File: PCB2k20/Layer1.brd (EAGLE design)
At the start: 173.9 x 196 mm, 242 parts, among them J1 XT30PB-F, Q1M1 AOD482, Q1M2 AOD482, Q1M3 AOD482, Q1M4 AOD482, U1M1 VNH5019, U1M2 VNH5019, U1M3 VNH5019, U1M4 VNH5019

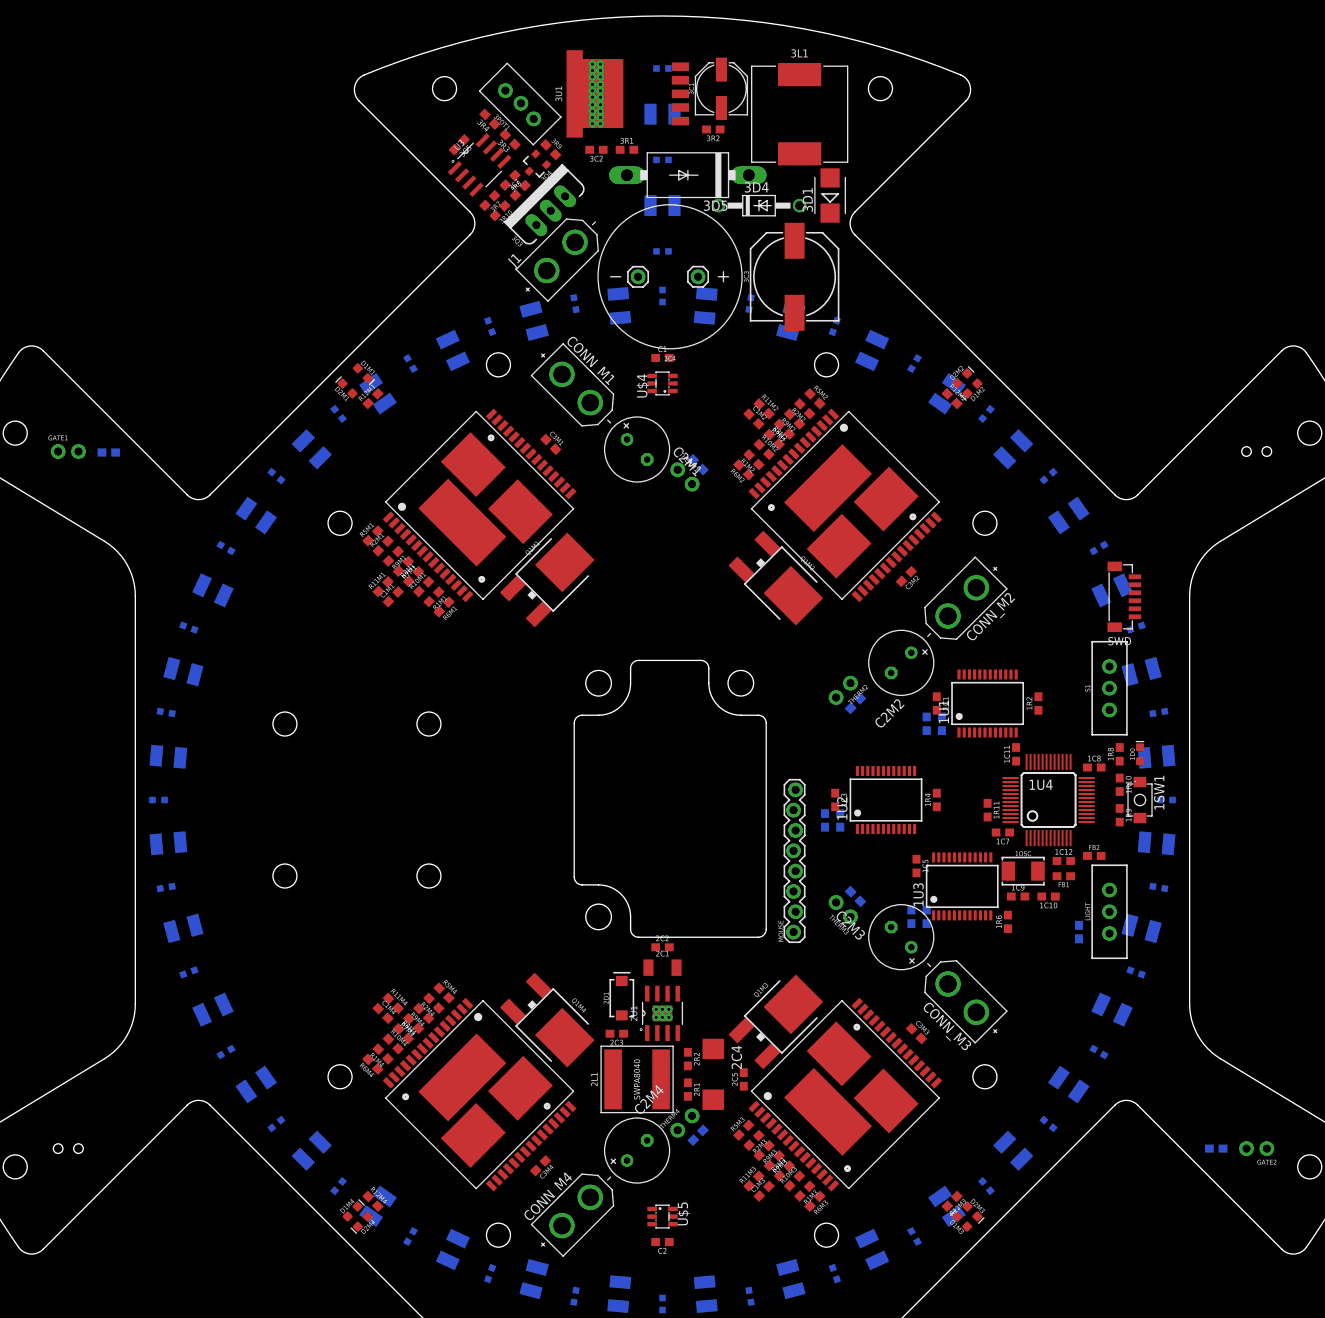
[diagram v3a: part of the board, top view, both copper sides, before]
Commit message: half routed
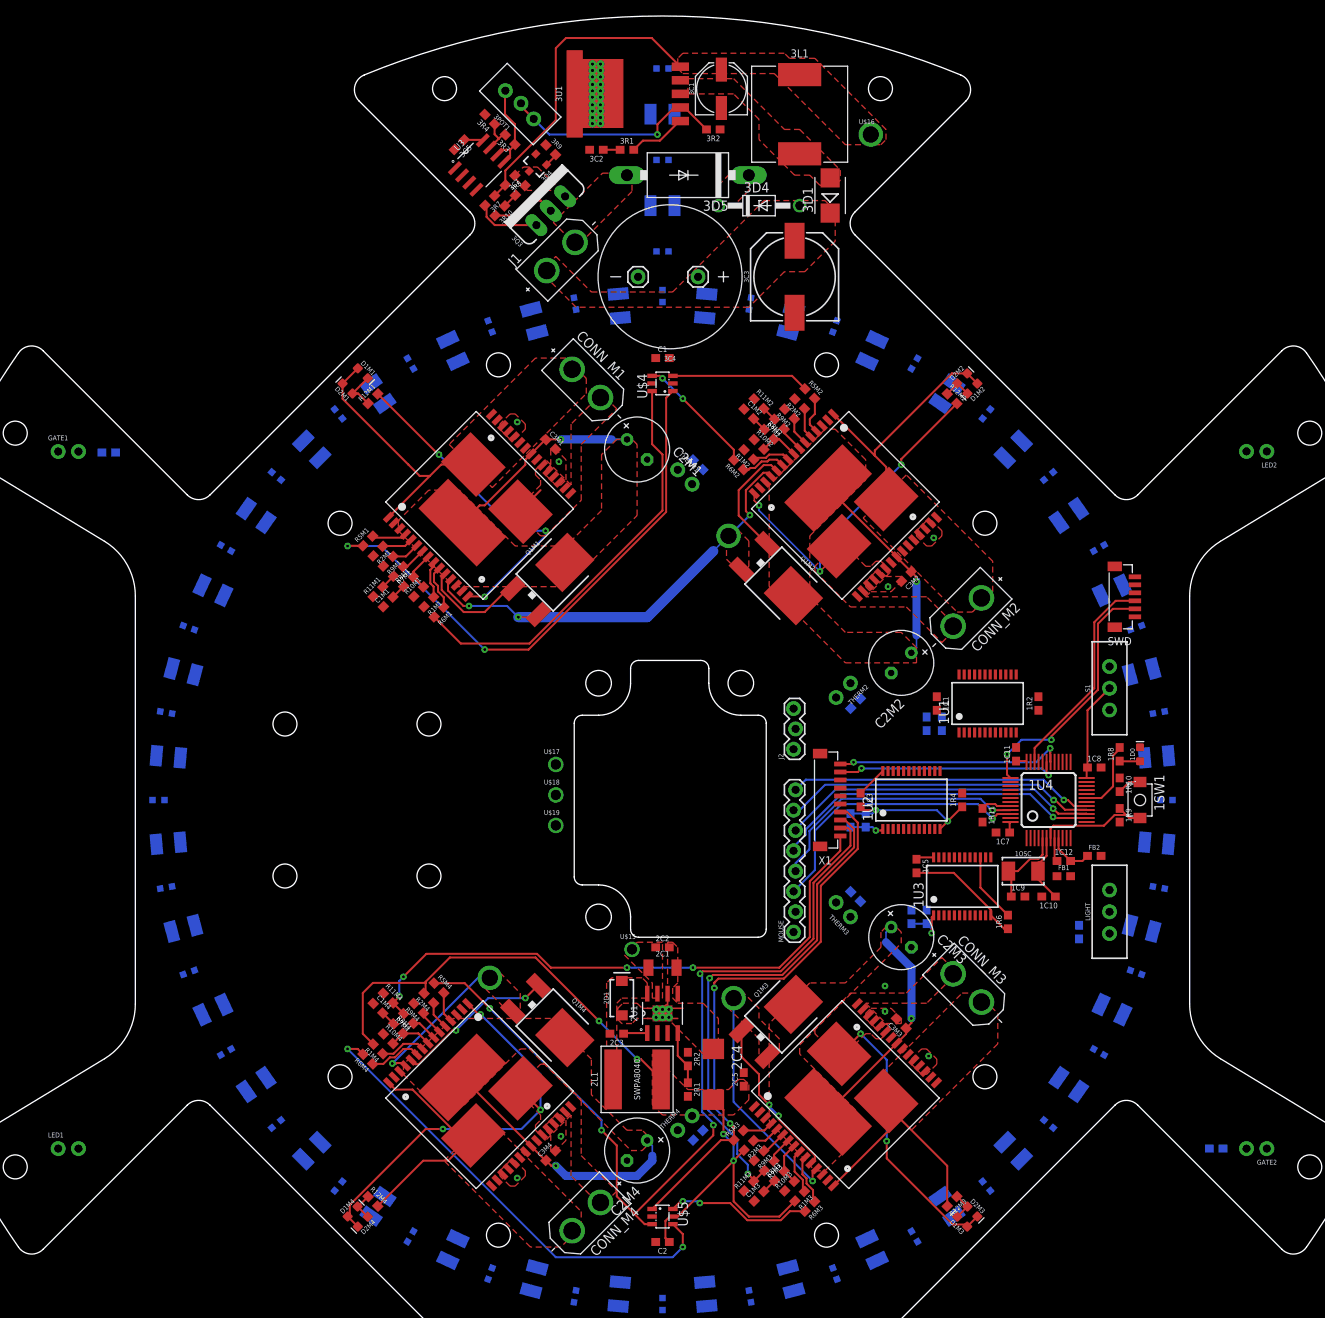
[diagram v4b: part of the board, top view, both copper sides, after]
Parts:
- added J2: CONN_03, JH:1X03_LOCK
- added J3, J4, J5, U$16: 14AWG, JH:14AWG
- added LED1, LED2: (no value), SparkFun-Connectors:1X02_NO_SILK
- added U$15, U$17, U$18, U$19: 18AWG, JH:18AWG
- added X1: BM10B-SRSS-TB, con-JST SH:BM10B-SRSS-TB
- moved 1R4 3.18 mm to (37.5, 0.00)
- moved 1C3 3.18 mm to (24.8, 0.00)
- moved 1R5 3.18 mm to (23.5, -2.54)
- moved 1C4 3.17 mm to (25.4, -2.54)
- moved 1U2 3.17 mm to (31.1, 0.00)
- moved C3M3 2.29 mm to (29.8, -27.9), turned to 135 degrees
- moved C3M4 1.80 mm to (-14.0, -44.5), turned to 45 degrees
- moved CONN_M1 1.42 mm to (-9.53, 52.1)
- moved CONN_M2 1.42 mm to (38.1, 23.5)
- moved CONN_M3 1.42 mm to (38.1, -23.5), turned to 315 degrees
- moved CONN_M4 1.42 mm to (-9.53, -52.1), turned to 225 degrees
- moved C1M4 0.90 mm to (-35.6, -26.0)
- moved R11M1 0.90 mm to (-35.6, 26.0)
- moved R1M4 0.90 mm to (-35.6, -31.1)
- moved R2M1 0.90 mm to (-35.6, 31.1), turned to 225 degrees
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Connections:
- new net LIGHT_INT: J2.1
- net 12V: now also U$15.P$1; no longer 3R7.1, 3R8.2
- net 3.3V: now also J2.3
- net GND: now also J2.2, LED1.2, LED2.2, U$18.P$1
- net INM1: now also X1.8
- net INM2: now also X1.6
- net INM3: now also X1.4
- net INM4: now also X1.2
- net MOUSE_MOT: now also 1U4.45
- net MOUSE_RST: now also 1U4.46
- net N$1: now also LED1.1, LED2.1, U$17.P$1
- net PWMM1: now also X1.7
- net PWMM2: now also X1.5
- net PWMM3: now also X1.3
- net PWMM4: now also X1.1
- net RX: now also X1.9
- net TX: now also X1.10
- net VCCA: now also U$19.P$1
- net VCC_1: now also 3R7.1, 3R8.2, J3.P$1, J4.P$1, J5.P$1, U$16.P$1
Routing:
- net VCC_1: track 0.00 -> 142.9 mm, vias 0 -> 5
- net INM4: track 0.00 -> 111.8 mm, vias 0 -> 4
- net 3.3V: track 0.00 -> 95.5 mm, vias 0 -> 4
- net PWMM4: track 0.00 -> 74.1 mm, vias 0 -> 4
- net INM1: track 0.00 -> 69.7 mm, vias 0 -> 2
- net INM3: track 0.00 -> 69.5 mm, vias 0 -> 2
- net PWMM3: track 0.00 -> 63.1 mm, vias 0 -> 2
- net INBM4: track 0.00 -> 58.8 mm, vias 0 -> 2
- net OUTAM4: track 0.00 -> 53.1 mm, vias 0 -> 3
- net INBM1: track 0.00 -> 52.3 mm
- net OUTBM1: track 0.00 -> 45.4 mm, vias 0 -> 3
- net OUTBM2: track 0.00 -> 45.4 mm, vias 0 -> 3
- net MOUSE_SS: track 0.00 -> 41.5 mm, vias 0 -> 1
- net MOUSE_SCK: track 0.00 -> 39.9 mm, vias 0 -> 1
- net MOUSE_MISO: track 0.00 -> 39.3 mm, vias 0 -> 1
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- added copper zone on layer 1, net 12V
- added copper zone on layer 1, net 3.3V
- added copper zone on layer 1, net GND
- added copper zone on layer 1, net N$101
- added copper zone on layer 1, net N$58
- added copper zone on layer 1, net N$66
- added copper zone on layer 1, net N$74
- added copper zone on layer 1, net N$82
- added copper zone on layer 1, net N$90
- added copper zone on layer 1, net N$95
- added copper zone on layer 1, net N$97
- added copper zone on layer 1, net OUTAM1
- added copper zone on layer 1, net OUTAM2
- added copper zone on layer 1, net OUTAM3
- added copper zone on layer 1, net OUTAM4
- added copper zone on layer 1, net OUTBM1
- added copper zone on layer 1, net OUTBM2
- added copper zone on layer 1, net OUTBM3
- added copper zone on layer 1, net OUTBM4
- added copper zone on layer 1, net SOLENOIDGND
- added copper zone on layer 1, net VCC_1
- added copper zone on layer 1, net VCC_2
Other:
- outline, holes or cut-outs redrawn

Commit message: done just need to silkscreen now!!!
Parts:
- removed 1D37, 1D39: 3528LED, JH:3528
- removed 1PT39, 1PT40, 1PT41, 1PT42: LIGHT_SENSORALS, SparkFun-Sensors:ALS-PT19
- removed 3C5: 0.1uF, JH:C0603
- removed 3R3: 10k, JH:R0603
- removed U3: (no value), JH:SOIC-8
- added 1C13, 1C14, 1C15, 1C16, 1C17: (no value), JH:C0603
- added 1R12, 1R13, 1R14, 1R15, 1R16: (no value), JH:R0603
- added C3: 1uF, JH:C0603
- added J10, J11, J13, J14, J15, J16, J17, J18, J19, J20, J6, J7, J8, J9: 14AWG, JH:14AWG
- added J12: (no value), SparkFun-Connectors:1X01
- added U$21, U$22, U$23, U$24, U$25, U$27, U$28: 18AWG, JH:18AWG
- added U$26: XT60XT60PB-M, JH:XT60PB-M
- 3R4: value 47(+5)k -> 57k
- J2: value CONN_03 -> (none); device JH:1X03_LOCK -> SparkFun-Connectors:1X04
- moved 1PT38 171.4 mm to (0.00, -91.4)
- moved 1C3 67.2 mm to (-29.2, -40.0), flipped to the bottom, turned to 90 degrees
- moved 1R4 66.6 mm to (-17.1, -38.1), flipped to the bottom, turned to 270 degrees
- moved 1U2 66.4 mm to (-22.9, -38.7), flipped to the bottom, turned to 180 degrees
- moved 1C4 65.8 mm to (-31.1, -36.2), turned to 270 degrees
- moved 1R5 62.5 mm to (-29.2, -36.2), turned to 90 degrees
- moved 1R7 25.4 mm to (51.4, -29.8), turned to 180 degrees
- moved 1PT37 22.9 mm to (0.00, 91.4)
- moved 1C6 22.7 mm to (51.4, -27.9), turned to 0 degrees
- moved R2 17.3 mm to (18.4, -69.2), turned to 270 degrees
- moved 1R3 17.1 mm to (49.5, 14.0)
- moved R1 16.3 mm to (21.0, -69.2), turned to 270 degrees
- moved 1C1 15.1 mm to (47.6, 19.1), flipped to the bottom
- moved 1C2 13.5 mm to (47.6, 14.0)
- moved 1R2 11.7 mm to (36.2, 16.5), flipped to the bottom
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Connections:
- removed net N$106: GATE1.2, R3.2
- removed net N$107: GATE2.2, R4.2
- removed net N$41: 1PT34.E, 1U3.17
- removed net N$42: 1PT35.E, 1U3.18
- removed net N$43: 1PT36.E, 1U3.19
- removed net N$44: 1PT37.E, 1U3.20
- removed net N$45: 1PT38.E, 1U3.21
- removed net N$46: 1PT39.E, 1U3.22
- removed net N$47: 1PT40.E, 1U3.23
- removed net N$48: 1PT41.E, 1U3.2
- removed net N$49: 1PT42.E, 1U3.3
- removed net N$50: 1U3.4, R5.1, THERM1.2
- removed net N$51: 1U3.5, R6.1, THERM2.2
- removed net N$52: 1U3.6, R7.1, THERM3.2
- removed net N$53: 1U3.7, R8.1, THERM4.2
- removed net N$54: 1U3.8, R3.1
- removed net N$55: 1U3.9, R4.1
- removed net N$93: 3POT1.3, 3R3.1, U3.5, U3.6
- removed net N$94: 3R3.2, 3R4.1, U3.7
- removed net POT_MOSI: 1U4.28, U3.3
- removed net POT_SCK: 1U4.26, U3.2
- removed net POT_SS: 1U4.25, U3.1
- new net GATE1: 1U3.21, GATE1.2, R3.2
- new net GATE2: 1U3.9, GATE2.2, R4.2
- new net L3>L1: J7.P$1, U$21.P$1, U$26.+
- new net M1+2: J5.P$1, Q1M1.3, Q1M2.3, U1M1.P12, U1M2.P12
- new net MOTOR_SW: J10.P$1, J11.P$1, J20.P$1, J8.P$1, J9.P$1, R1.2
- new net N$2: 1PT26.E, 1U2.16
- new net N$22: 1PT8.E, 1U1.18
- new net N$39: J3.P$1, Q1M4.3, U1M4.P12
- new net PT22: 1C6.1, 1PT22.E, 1R7.2, 1U3.8
- new net PT23: 1C13.1, 1PT23.E, 1R12.2, 1U3.7
- new net PT24: 1C14.1, 1PT24.E, 1R13.2, 1U3.6
- new net PT25: 1C15.1, 1PT25.E, 1R14.2, 1U3.5
- new net PT37: 1C16.1, 1PT37.E, 1R15.2, 1U3.19
- new net PT38: 1C17.1, 1PT38.E, 1R16.2, 1U3.4
- new net THERM1: 1U3.18, R5.2, THERM1.2
- new net THERM2: 1U3.16, R6.2, THERM2.2
- new net THERM3: 1U3.23, R7.2, THERM3.2
- new net THERM4: 1U3.22, R8.2, THERM4.2
- net 3.3V: now also J2.4, U$28.P$1; no longer 3C5.1, LIGHT.2, U3.8
- net AGND: now also 1C13.2, 1C14.2, 1C15.2, 1C16.2, 1C17.2, 1R12.1, 1R13.1, 1R14.1, 1R15.1, 1R16.1, R3.1, R4.1, R5.1, R6.1, R7.1, R8.1
- net BATT_LVL: now also 1U4.2
- net CSM1: now also 1U3.20
- net CSM2: now also 1U3.17
- net CSM3: now also 1U3.2
- net CSM4: now also 1U3.3
- net GND: now also C3.2, J12.1, J13.P$1, J14.P$1, J15.P$1, J16.P$1, J17.P$1, J18.P$1, J19.P$1, J6.P$1, U$23.P$1, U$25.P$1, U$26.-; no longer 1D37.C, 1D39.C, 3C5.2, U3.4
- net LIGHT_INT: now also 1U4.32
- net LSOUT1: now also 1U4.18
- net LSOUT2: now also 1U4.11
- net LSOUT3: now also 1U4.10; no longer 1C6.1, 1R7.2
- net N$1: now also C3.1, U$22.P$1; no longer 1D37.A, 1D39.A
- net N$10: now also 1PT33.E, 1U2.23; no longer 1PT7.E, 1U1.22
- net N$11: now also 1PT34.E, 1U2.2; no longer 1PT8.E, 1U1.23
- net N$12: now also 1PT35.E, 1U2.3; no longer 1PT9.E, 1U1.2
- net N$13: now also 1PT36.E, 1U2.4; no longer 1PT10.E, 1U1.3
- net N$14: now also 1PT1.E, 1U2.5; no longer 1PT11.E, 1U1.4
- net N$15: now also 1PT2.E, 1U2.6; no longer 1PT12.E, 1U1.5
- net N$16: now also 1PT3.E, 1U2.7; no longer 1PT13.E, 1U1.6
- net N$17: now also 1PT4.E, 1U2.8; no longer 1PT14.E, 1U1.7
- net N$18: now also 1PT5.E, 1U2.9; no longer 1PT15.E, 1U1.8
- net N$19: now also 1PT6.E, 1U1.16; no longer 1PT16.E, 1U1.9
- net N$21: now also 1PT7.E, 1U1.17; no longer 1PT17.E, 1U2.16
- net N$23: now also 1PT9.E, 1U1.19; no longer 1PT18.E, 1U2.17
- net N$24: now also 1PT10.E, 1U1.20; no longer 1PT19.E, 1U2.18
- net N$25: now also 1PT11.E, 1U1.21; no longer 1PT20.E, 1U2.19
- net N$26: now also 1PT12.E, 1U1.22; no longer 1PT21.E, 1U2.20
- net N$27: now also 1PT13.E, 1U1.23; no longer 1PT22.E, 1U2.21
- net N$28: now also 1PT14.E, 1U1.2; no longer 1PT23.E, 1U2.22
- net N$29: now also 1PT15.E, 1U1.3; no longer 1PT24.E, 1U2.23
- net N$30: now also 1PT16.E, 1U1.4; no longer 1PT25.E, 1U2.2
- net N$31: now also 1PT17.E, 1U1.5; no longer 1PT26.E, 1U2.3
- net N$32: now also 1PT18.E, 1U1.6; no longer 1PT27.E, 1U2.4
- net N$33: now also 1PT19.E, 1U1.7; no longer 1PT28.E, 1U2.5
- net N$34: now also 1PT20.E, 1U1.8; no longer 1PT29.E, 1U2.6
- net N$35: now also 1PT21.E, 1U1.9; no longer 1PT30.E, 1U2.7
- net N$36: now also LIGHT.2, U$27.P$1; no longer 1PT31.E, 1U2.8
- net N$37: now also 3POT1.3, 3R4.1; no longer 1PT32.E, 1U2.9
- net N$4: now also 1PT27.E, 1U2.17; no longer 1PT1.E, 1U1.16
- net N$40: now also J4.P$1, Q1M3.3, U1M3.P12; no longer 1PT33.E, 1U3.16
- net N$5: now also 1PT28.E, 1U2.18; no longer 1PT2.E, 1U1.17
- net N$6: now also 1PT29.E, 1U2.19; no longer 1PT3.E, 1U1.18
- net N$7: now also 1PT30.E, 1U2.20; no longer 1PT4.E, 1U1.19
- net N$8: now also 1PT31.E, 1U2.21; no longer 1PT5.E, 1U1.20
- net N$9: now also 1PT32.E, 1U2.22; no longer 1PT6.E, 1U1.21
- net S0: now also 1U4.38
- net S1: now also 1U4.39
- net S2: now also 1U4.40
- net S3: now also 1U4.41
- net SOLENOIDON: now also 1U4.29
- net VCCA: now also U$24.P$1; no longer 1PT39.C, 1PT40.C, 1PT41.C, 1PT42.C, R5.2, R6.2, R7.2, R8.2
- net VCC_1: no longer J3.P$1, J4.P$1, J5.P$1, Q1M1.3, Q1M2.3, Q1M3.3, Q1M4.3, R1.2, U1M1.P12, U1M2.P12, U1M3.P12, U1M4.P12
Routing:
- net VCCA: track 12.0 -> 760.0 mm, vias 0 -> 24
- net N$1: track 0.00 -> 576.0 mm, vias 0 -> 6
- net AGND: track 36.6 -> 566.0 mm, vias 2 -> 21
- net 3.3V: track 95.5 -> 330.9 mm, vias 4 -> 17
- net S2: track 0.00 -> 146.8 mm, vias 0 -> 6
- net GATE1: track 0.00 -> 144.3 mm, vias 0 -> 4
- net S1: track 0.00 -> 143.7 mm, vias 0 -> 8
- net S3: track 0.00 -> 133.8 mm, vias 0 -> 9
- net PT37: track 0.00 -> 132.6 mm, vias 0 -> 3
- net LSOUT2: track 4.30 -> 135.8 mm, vias 1 -> 3
- net S0: track 0.00 -> 129.3 mm, vias 0 -> 8
- net SOLENOIDON: track 1.74 -> 125.1 mm, vias 0 -> 6
- net PT38: track 0.00 -> 120.7 mm, vias 0 -> 3
- net N$19: track 0.00 -> 111.0 mm
- net VCC_1: track 142.9 -> 39.2 mm, vias 5 -> 0
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- added copper zone on layer 16, net GND
- added copper zone on layer 1, net L3>L1
- added copper zone on layer 16, net L3>L1
- added copper zone on layer 1, net M1+2
- added copper zone on layer 1, net MOTOR_SW
- added copper zone on layer 16, net MOTOR_SW
- added copper zone on layer 1, net N$39
- added copper zone on layer 1, net N$40
- added copper zone on layer 16, net VCC_2
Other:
- board text added: "gnd via"

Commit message: add gerbers, please everything turn out well!
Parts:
- added J21, U$29: 14AWG, JH:14AWG
- 2L1: value SWPA8040/10uH -> 10uH
- 3C4: value 1500uF -> 1000uF/63V
- moved U$21 2.54 mm to (-11.4, -68.6)
- moved J12 2.54 mm to (-17.1, -73.0)
- moved J7 2.54 mm to (-11.4, -73.0)
- moved U$26 1.91 mm to (0.00, -69.2)
- moved 3R2 1.09 mm to (5.26, 83.9)
- moved J13 0.63 mm to (14.0, -73.7)
- moved J6 0.63 mm to (9.53, -73.7)
- flipped 3R4 to the bottom, turned to 315 degrees
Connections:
- net GND: now also J21.P$1, U$29.P$1
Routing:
- net 3.3V: track 330.9 -> 355.0 mm, vias 17 -> 18
- net VCC_2: track 18.4 -> 17.5 mm
- net FDBK: track 28.7 -> 28.2 mm
- net GND: vias 60 -> 65
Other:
- outline, holes or cut-outs redrawn
- board text added: "12v"
- board text added: "12v to 3v3 buck"
- board text added: "3v3"
- board text added: "3v3 out"
- board text added: "3v3in"
- board text added: "Team Transcendence @bozotics github.com/hcbozo robo.infocommsociety.com"
- board text added: "gnd"
- board text added: "gnd to 3v3 buck"
- board text added: "int"
- board text added: "light"
- board text added: "lightout"
- board text added: "miso"
- board text added: "mosi"
- board text added: "mot"
- board text added: "motor connections"
- board text added: "off"
- board text added: "on"
- board text added: "prog power"
- board text added: "rst"
- board text added: "sck"
- board text added: "ss"
- board text added: "switch input"
- board text added: "switch led gnd"
- board text added: "switch output"
- board text added: "vcca"

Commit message: update values
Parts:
- 1C1, 1C3, 1C5: value (none) -> 0.1uF
- 1C13, 1C14, 1C15, 1C16, 1C17, 1C2, 1C4, 1C6: value (none) -> 1uF
- 1R1: value 15 -> 0.39
- 1R12, 1R13, 1R14, 1R15, 1R16, 1R3, 1R5, 1R7: value (none) -> 3k
- 1R2, 1R4, 1R6: value (none) -> 10k
- 2C4: value 220uF -> 330uF
- 2D1: value 3A/40V/500mV -> SS54
- C3M1, C3M2, C3M3, C3M4: value 1.0uF -> 1uF
- R1: value 300k -> 30k
- R11M1, R11M2, R11M3, R11M4, R2: value 100k -> 10k
- R3, R4: value (none) -> 4.7k
- R5, R6, R7, R8: value (none) -> 3.9k
